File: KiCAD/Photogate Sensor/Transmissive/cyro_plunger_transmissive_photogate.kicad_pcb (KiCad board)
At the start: 2 copper layers, 122 x 70 mm, 58 parts, among them J2 FFC Socket, J3 USB_B_Micro, J4 UPDI socket, J5 DC Jack, J6 Conn_01x03_Socket, J7 USB_B_Micro, J8 FFC Socket, J9 Conn_01x03_Socket, Q1 Q_NMOS_GSD, Q2 Q_NMOS_GSD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

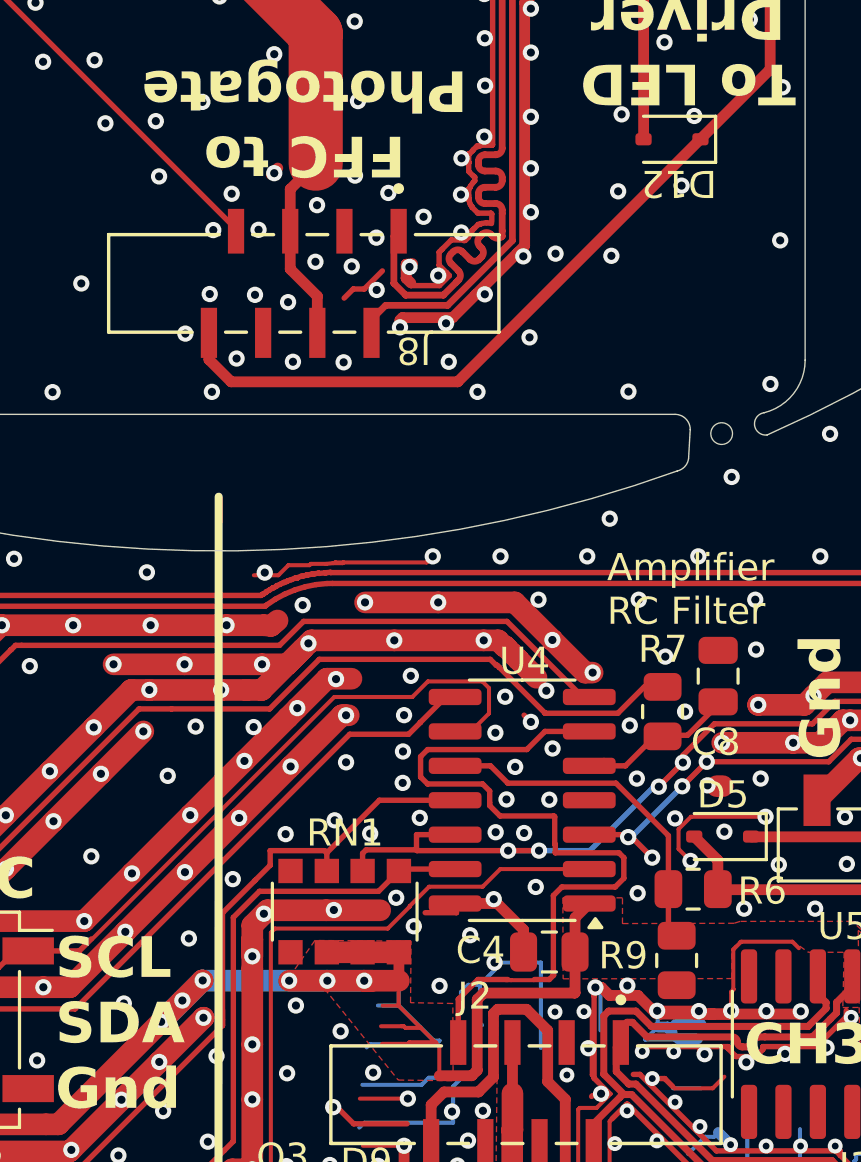
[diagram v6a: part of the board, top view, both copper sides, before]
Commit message: Interrupt sync working
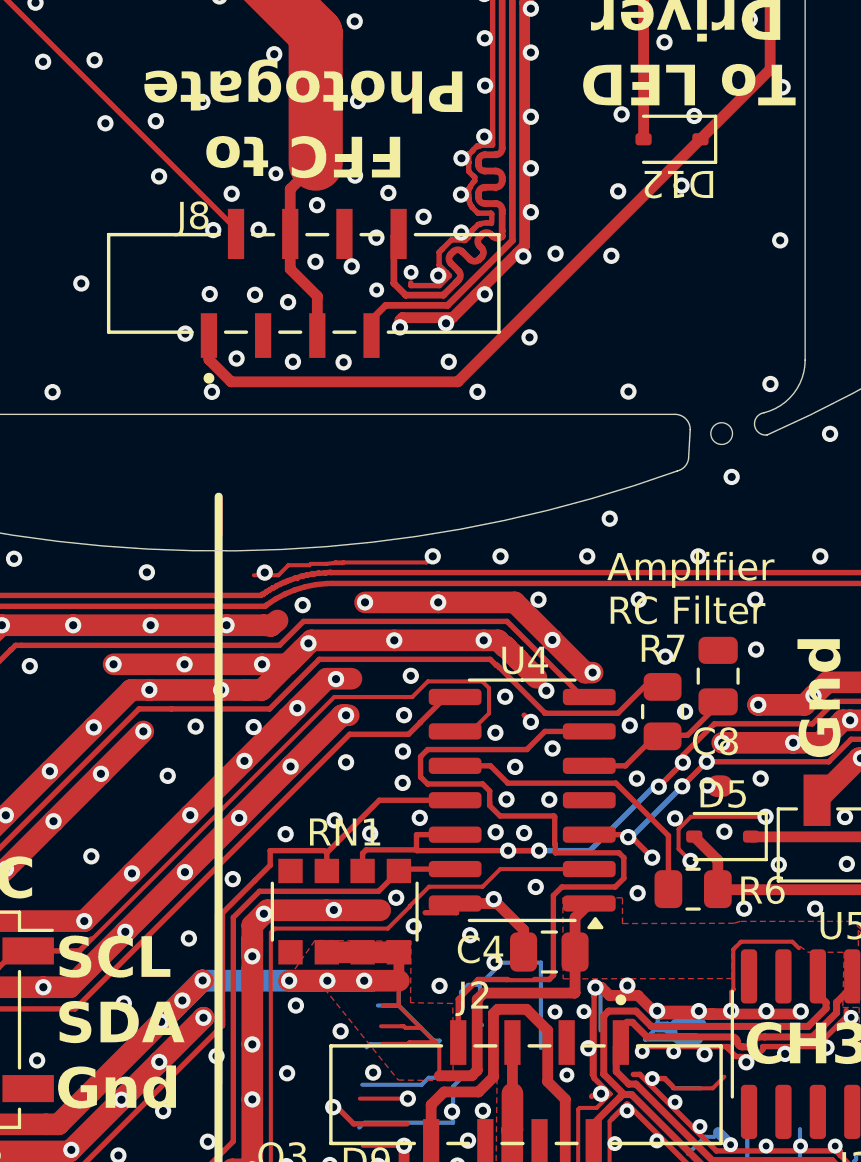
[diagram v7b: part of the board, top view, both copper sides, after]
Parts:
- removed R9: 47k, Resistor_SMD:R_0805_2012Metric
- turned J8 to 0 degrees
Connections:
- J8 pad 1: /D+ -> /Vusb
- J8 pad 2: /D- -> /Comp Out
- J8 pad 7: /Comp Out -> /D-
- J8 pad 8: /Vusb -> /D+
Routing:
- net GND: track 888.9 -> 885.7 mm
- net /UPDI: track 12.8 -> 10.9 mm

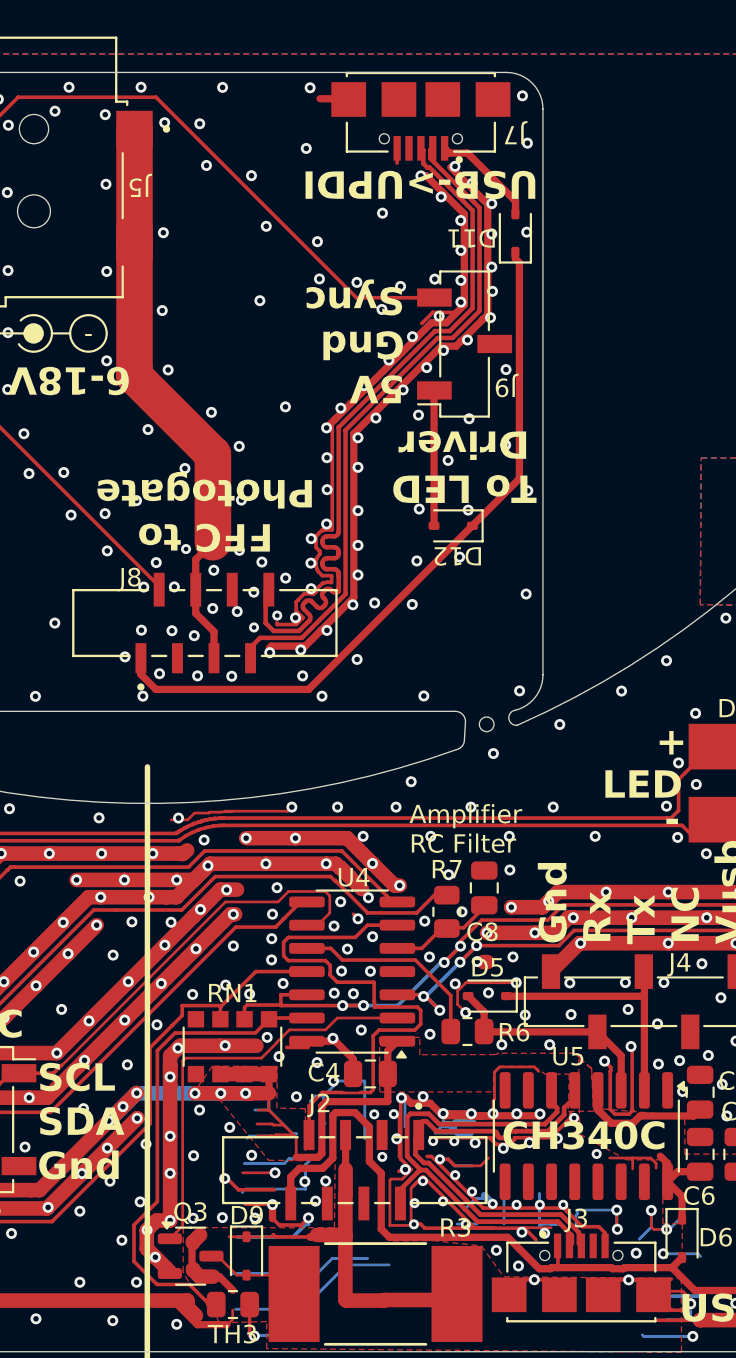
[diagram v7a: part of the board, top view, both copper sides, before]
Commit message: Remove second USB connector
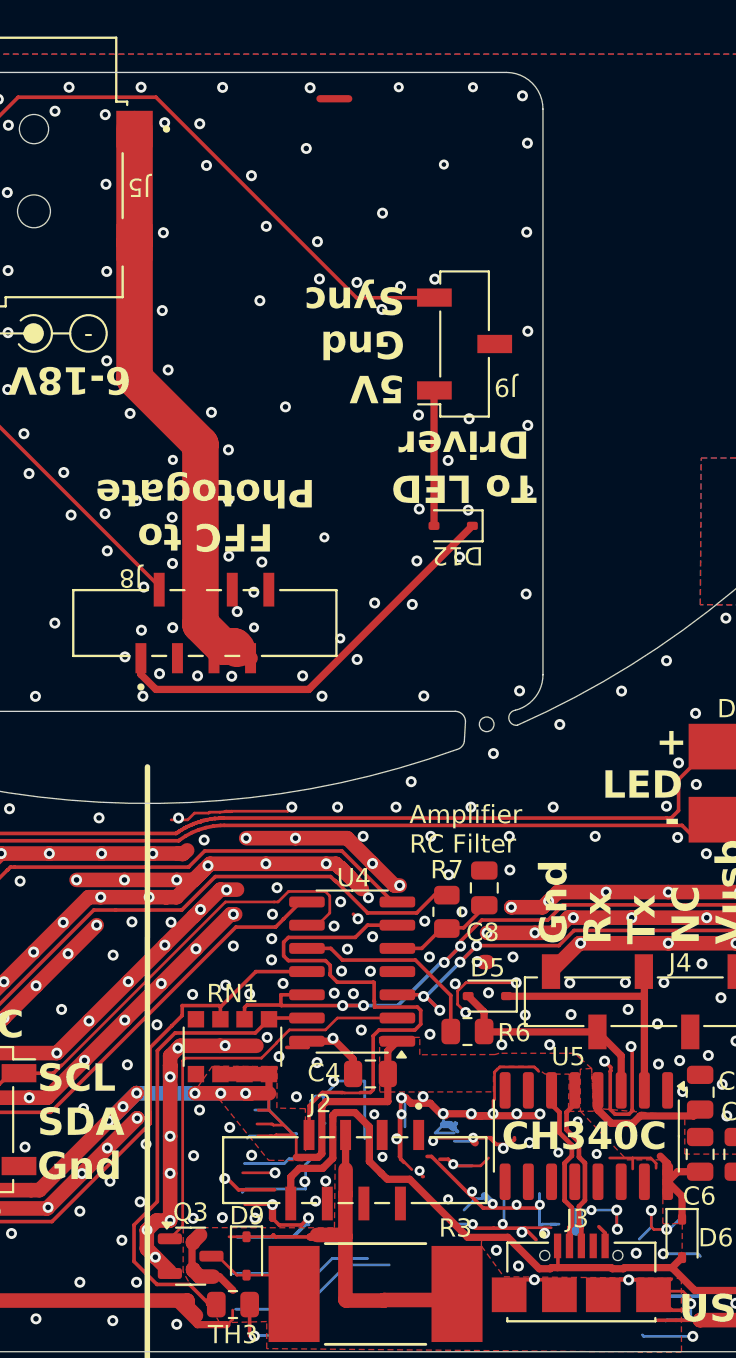
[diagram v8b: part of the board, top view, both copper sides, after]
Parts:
- removed D11: D_Schottky, Diode_SMD:D_SOD-323
- removed J7: USB_B_Micro, Custom:CUI_UJ2-MIBH-G-SMT-TR
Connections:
- J2 pad 1: /D+ -> GND
- J2 pad 2: /D- -> +12V
- J8 pad 7: /D- -> +12V
- J8 pad 8: /D+ -> GND
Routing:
- net GND: track 885.7 -> 789.7 mm, vias 738 -> 693
- net /D+: track 64.6 -> 8.44 mm
- net /D-: track 62.1 -> 8.46 mm
- net /Vusb: track 118.9 -> 101.0 mm
- net Net-(D11-A): track 5.77 -> 0.00 mm
- net +12V: track 245.7 -> 246.9 mm
